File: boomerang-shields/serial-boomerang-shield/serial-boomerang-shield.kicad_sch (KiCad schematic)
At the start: 11 parts, among them J1 Power output header, J10 Pin Socket D, J2 USBasp header, J3 Port A, J4 Port B, J5 Port C, J6 Port D, J7 Pin Socket A, J8 Pin Socket B, J9 Pin Socket C

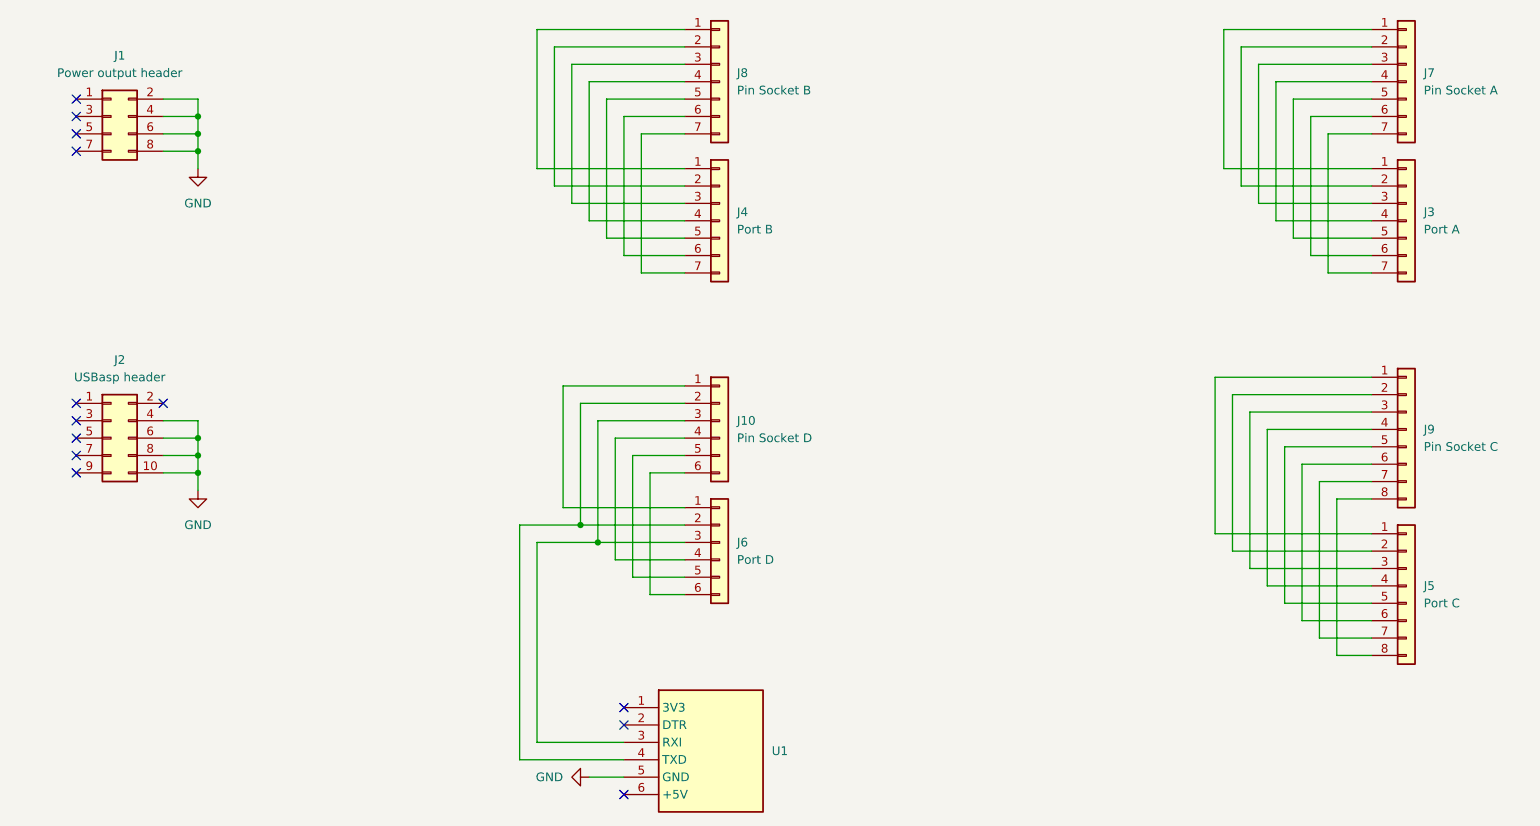
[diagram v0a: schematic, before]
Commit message: Serial Boomerang Shield updated, power output header added
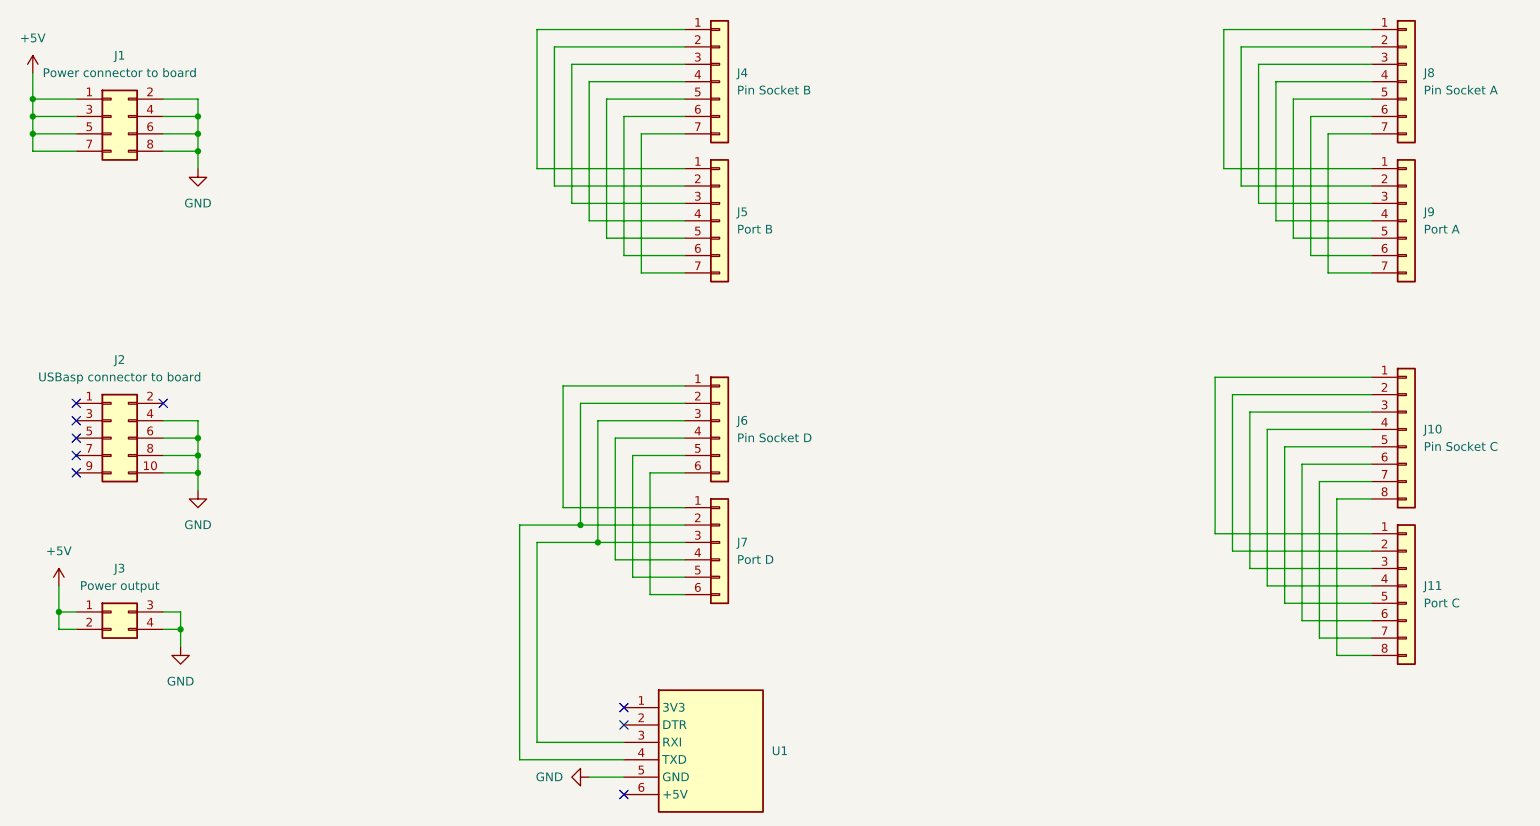
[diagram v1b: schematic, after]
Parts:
- added J3: Power output, Connector_PinSocket_2.54mm:PinSocket_2x02_P2.54mm_Vertical, symbol Connector_Generic:Conn_02x02_Top_Bottom
- J1: value Power output header -> Power connector to board
- J2: value USBasp header -> USBasp connector to board
- renumbered J9 to J10, J5 to J11, J8 to J4, J4 to J5, J10 to J6, J6 to J7, J7 to J8, J3 to J9
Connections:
- net GND: now also J3.3 (Pin_3), J3.4 (Pin_4)
- net +5V: now reaches J1.1 (Pin_1)
- net +5V: now also J1.3 (Pin_3), J1.5 (Pin_5), J1.7 (Pin_7), J3.1 (Pin_1), J3.2 (Pin_2)
- no-connect marks 13 -> 9
